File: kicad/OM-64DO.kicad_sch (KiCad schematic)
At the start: 30 parts, among them J101 15EDGVC-3.5-4P, J102 02x03 1.27, J201 15EDGVC-3.5-20P, J301 15EDGVC-3.5-20P, J401 15EDGVC-3.5-20P, J501 15EDGVC-3.5-20P, U101 R-78E3.3-0.5, U102 THVD1450DRBR, U103 STM32G031F8P6

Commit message: feat: add LCSC parts numbers
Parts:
- C101, C102: LCSC# (none) -> C417124; Mouser Part Number 81-GRT31CR61H106KE1L -> (none); Mouser# (none) -> 81-GRT31CR61H106KE1L
- C103, C105, C106: LCSC# (none) -> C161115; Mouser Part Number 81-GCJ188R71H104KA2D -> (none); Mouser# (none) -> 81-GCJ188R71H104KA2D
- C104: LCSC# (none) -> C668370; Mouser Part Number 81-GRT188R61H225KE3D -> (none); Mouser# (none) -> 81-GRT188R61H225KE3D
- D101: LCSC# (none) -> C172881; Mouser Part Number 576-SM712-02HTG -> (none); Mouser# (none) -> 576-SM712-02HTG
- D102: LCSC# (none) -> C364560; Mouser Part Number 859-LTST-C190EKT -> (none); Mouser# (none) -> 859-LTST-C190EKT
- D103: LCSC# (none) -> C6877135; Mouser Part Number 652-CD123D-B140LR -> (none); Mouser# (none) -> 652-CD123D-B140LR
- D104: LCSC# (none) -> C148227; Mouser Part Number 576-SMAJ28A -> (none); Mouser# (none) -> 576-SMAJ28A
- F101: LCSC# (none) -> C151133; Mouser Part Number 576-0466.500NR -> (none); Mouser# (none) -> 576-0466.500NR
- J101: LCSC# (none) -> C22380434
- J201, J301, J401, J501: LCSC# (none) -> C5188336
- R101, R102: LCSC# (none) -> C4297913; Mouser Part Number 667-ERJ-H3EF1002V -> (none); Mouser# (none) -> 667-ERJ-H3EF1002V
- R103: LCSC# (none) -> C491199; Mouser Part Number 667-ERJ-UP3J471V -> (none); Mouser# (none) -> 667-ERJ-UP3J471V
- U101: LCSC# (none) -> C18212316; Mouser Part Number 919-R-78E3.3-0.5 -> (none); Mouser# (none) -> 919-R-78E3.3-0.5
- U102: LCSC# (none) -> C1850226; Mouser Part Number 595-THVD1450DRBR -> (none); Mouser# (none) -> 595-THVD1450DRBR
- U103: LCSC# (none) -> C529334; Mouser Part Number 511-STM32G031F8P6 -> (none); Mouser# (none) -> 511-STM32G031F8P6
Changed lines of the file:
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@@
 			)
 		)
-		(property "Mouser Part Number" "81-GCJ188R71H104KA2D"
+		(property "LCSC#" "C161115"
+			(at 58.42 138.43 90)
+			(effects
+				(font
+					(size 1.27 1.27)
+				)
+				(hide yes)
+			)
+		)
+		(property "Mouser#" "81-GCJ188R71H104KA2D"
 			(at 58.42 138.43 90)
 			(effects
@@
 			)
 		)
-		(property "Mouser Part Number" "81-GCJ188R71H104KA2D"
+		(property "LCSC#" "C161115"
+			(at 186.69 201.93 0)
+			(effects
+				(font
+					(size 1.27 1.27)
+				)
+				(hide yes)
+			)
+		)
+		(property "Mouser#" "81-GCJ188R71H104KA2D"
 			(at 186.69 201.93 0)
 			(effects
@@
 			)
 		)
-		(property "Mouser Part Number" ""
+		(property "LCSC#" ""
 			(at 53.34 87.63 0)
 			(effects
@@
 			)
 		)
-		(property "Mouser Part Number" ""
+		(property "LCSC#" "C5188336"
 			(at 270.51 114.3 0)
 			(effects
@@
 			)
 		)
-		(property "Mouser Part Number" "81-GCJ188R71H104KA2D"
+		(property "LCSC#" "C161115"
+			(at 138.43 115.57 0)
+			(effects
+				(font
+					(size 1.27 1.27)
+				)
+				(hide yes)
+			)
+		)
+		(property "Mouser#" "81-GCJ188R71H104KA2D"
 			(at 138.43 115.57 0)
 			(effects
@@
 			)
 		)
-		(property "Mouser Part Number" "667-ERJ-UP3J471V"
+		(property "Part Number" "ERJ-UP3J471V"
 			(at 166.37 199.39 90)
 			(effects
@@
 			)
 		)
-		(property "Part Number" "ERJ-UP3J471V"
+		(property "LCSC#" "C491199"
+			(at 166.37 199.39 90)
+			(effects
+				(font
+					(size 1.27 1.27)
+				)
+				(hide yes)
+			)
+		)
+		(property "Mouser#" "667-ERJ-UP3J471V"
 			(at 166.37 199.39 90)
 			(effects
@@
 			)
 		)
-		(property "Mouser Part Number" "595-THVD1450DRBR"
+		(property "LCSC#" "C1850226"
+			(at 63.5 154.94 0)
+			(effects
+				(font
+					(size 1.27 1.27)
+				)
+				(hide yes)
+			)
+		)
+		(property "Mouser#" "595-THVD1450DRBR"
 			(at 63.5 154.94 0)
 			(effects
@@
 			)
 		)
-		(property "Mouser Part Number" "81-GRT31CR61H106KE1L"
+		(property "LCSC#" "C417124"
+			(at 129.54 201.93 0)
+			(effects
+				(font
+					(size 1.27 1.27)
+				)
+				(hide yes)
+			)
+		)
+		(property "Mouser#" "81-GRT31CR61H106KE1L"
 			(at 129.54 201.93 0)
 			(effects
@@
 			)
 		)
-		(property "Mouser Part Number" "81-GRT31CR61H106KE1L"
+		(property "LCSC#" "C417124"
+			(at 157.48 201.93 0)
+			(effects
+				(font
+					(size 1.27 1.27)
+				)
+				(hide yes)
+			)
+		)
+		(property "Mouser#" "81-GRT31CR61H106KE1L"
 			(at 157.48 201.93 0)
 			(effects
@@
 			)
 		)
-		(property "Mouser Part Number" ""
+		(property "LCSC#" ""
 			(at 53.34 106.68 0)
 			(effects
@@
 			)
 		)
-		(property "Mouser Part Number" "511-STM32G031F8P6"
+		(property "LCSC#" "C529334"
+			(at 167.64 124.46 0)
+			(effects
+				(font
+					(size 1.27 1.27)
+				)
+				(hide yes)
+			)
+		)
+		(property "Mouser#" "511-STM32G031F8P6"
 			(at 167.64 124.46 0)
 			(effects
@@
 			)
 		)
-		(property "Mouser Part Number" ""
+		(property "LCSC#" ""
 			(at 83.82 201.93 0)
 			(effects
@@
 			)
 		)
-		(property "Mouser Part Number" "576-SM712-02HTG"
+		(property "LCSC#" "C172881"
+			(at 81.28 149.86 90)
+			(effects
+				(font
+					(size 1.27 1.27)
+				)
+				(hide yes)
+			)
+		)
+		(property "Mouser#" "576-SM712-02HTG"
 			(at 81.28 149.86 90)
 			(effects
@@
 			)
 		)
-		(property "Sim.Pin" "1=K 2=A"
+		(property "Part Number" "LTST-C190EKT"
 			(at 166.37 204.47 0)
 			(effects
@@
 			)
 		)
-		(property "Part Number" "LTST-C190EKT"
+		(property "Manufacturer" "LITEON"
 			(at 166.37 204.47 0)
 			(effects
@@
 			)
 		)
-		(property "Mouser Part Number" "859-LTST-C190EKT"
+		(property "LCSC#" "C364560"
 			(at 166.37 204.47 0)
 			(effects
@@
 			)
 		)
-		(property "Manufacturer" "LITEON"
+		(property "Mouser#" "859-LTST-C190EKT"
 			(at 166.37 204.47 0)
 			(effects
@@
 			)
 		)
-		(property "Mouser Part Number" ""
+		(property "LCSC#" ""
 			(at 53.34 113.03 0)
 			(effects
@@
 			)
 		)
-		(property "Mouser Part Number" ""
-			(at 48.26 200.66 0)
+		(property "LCSC#" "C22380434"
+			(at 48.26 200.66 90)
 			(effects
 				(font
@@
 			)
 		)
-		(property "Mouser Part Number" ""
+		(property "LCSC#" ""
 			(at 53.34 93.98 0)
 			(effects
@@
 			)
 		)
-		(property "Mouser Part Number" "576-SMAJ28A"
+		(property "Part Number" "SMAJ28A"
 			(at 121.92 201.93 90)
 			(effects
@@
 			)
 		)
-		(property "Part Number" "SMAJ28A"
+		(property "LCSC#" "C148227"
+			(at 121.92 201.93 90)
+			(effects
+				(font
+					(size 1.27 1.27)
+				)
+				(hide yes)
+			)
+		)
+		(property "Mouser#" "576-SMAJ28A"
 			(at 121.92 201.93 90)
 			(effects
@@
 			)
 		)
-		(property "Mouser Part Number" "919-R-78E3.3-0.5"
+		(property "LCSC#" "C18212316"
+			(at 143.51 198.12 0)
+			(effects
+				(font
+					(size 1.27 1.27)
+				)
+				(hide yes)
+			)
+		)
+		(property "Mouser#" "919-R-78E3.3-0.5"
 			(at 143.51 198.12 0)
 			(effects
@@
 			)
 		)
-		(property "Mouser Part Number" ""
+		(property "LCSC#" "C5188336"
 			(at 270.51 215.9 0)
 			(effects
@@
 			)
 		)
-		(property "Mouser Part Number" "667-ERJ-H3EF1002V"
-			(at 50.8 165.1 0)
+		(property "LCSC#" "C4297913"
+			(at 50.8 165.1 90)
+			(effects
+				(font
+					(size 1.27 1.27)
+				)
+				(hide yes)
+			)
+		)
+		(property "Mouser#" "667-ERJ-H3EF1002V"
+			(at 50.8 165.1 90)
 			(effects
 				(font
@@
 			)
 		)
-		(property "Mouser Part Number" ""
+		(property "LCSC#" ""
 			(at 53.34 100.33 0)
 			(effects
@@
 			)
 		)
-		(property "Mouser Part Number" ""
+		(property "LCSC#" ""
 			(at 53.34 81.28 0)
 			(effects
@@
 			)
 		)
-		(property "Mouser Part Number" ""
+		(property "LCSC#" "C5188336"
 			(at 270.51 165.1 0)
 			(effects
@@
 			)
 		)
-		(property "Mouser Part Number" ""
+		(property "LCSC#" ""
 			(at 53.34 119.38 0)
 			(effects
@@
 			)
 		)
-		(property "Mouser Part Number" "576-0466.500NR"
+		(property "Part Number" "0466.500NR"
 			(at 111.76 198.12 0)
 			(effects
@@
 			)
 		)
-		(property "Part Number" "0466.500NR"
+		(property "LCSC#" "C151133"
+			(at 111.76 198.12 0)
+			(effects
+				(font
+					(size 1.27 1.27)
+				)
+				(hide yes)
+			)
+		)
+		(property "Mouser#" "576-0466.500NR"
 			(at 111.76 198.12 0)
 			(effects
@@
 			)
 		)
-		(property "Mouser Part Number" "652-CD123D-B140LR"
+		(property "Part Number" "CD123D-B140LR"
 			(at 118.11 198.12 0)
 			(effects
@@
 			)
 		)
-		(property "Part Number" "CD123D-B140LR"
+		(property "LCSC#" "C6877135"
+			(at 118.11 198.12 0)
+			(effects
+				(font
+					(size 1.27 1.27)
+				)
+				(hide yes)
+			)
+		)
+		(property "Mouser#" "652-CD123D-B140LR"
 			(at 118.11 198.12 0)
 			(effects
@@
 			)
 		)
-		(property "Mouser Part Number" "667-ERJ-H3EF1002V"
+		(property "LCSC#" "C4297913"
+			(at 223.52 44.45 90)
+			(effects
+				(font
+					(size 1.27 1.27)
+				)
+				(hide yes)
+			)
+		)
+		(property "Mouser#" "667-ERJ-H3EF1002V"
 			(at 223.52 44.45 90)
 			(effects
@@
 			)
 		)
-		(property "Mouser Part Number" ""
+		(property "LCSC#" "C5188336"
 			(at 270.51 63.5 0)
 			(effects
@@
 			)
 		)
-		(property "Mouser Part Number" "81-GRT188R61H225KE3D"
+		(property "LCSC#" "C668370"
+			(at 181.61 201.93 0)
+			(effects
+				(font
+					(size 1.27 1.27)
+				)
+				(hide yes)
+			)
+		)
+		(property "Mouser#" "81-GRT188R61H225KE3D"
 			(at 181.61 201.93 0)
 			(effects

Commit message: feat: reduce board size, update pcb design
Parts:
- U101: symbol Regulator_Switching:R-78E3.3-1.0 -> Converter_DCDC:R-78E3.3-0.5
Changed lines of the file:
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@@
 	(title_block
 		(title "OM-64DO - 64 CHANNEL OUTPUT EXPANSION MODULE (MAIN)")
-		(date "2026-03-09")
+		(date "2026-03-12")
 		(rev "1B")
 		(company "HTTPS://GITHUB.COM/OPENMODBUS/OM-64DO")
@@
 	)
 	(symbol
-		(lib_id "Regulator_Switching:R-78E3.3-1.0")
+		(lib_id "Converter_DCDC:R-78E3.3-0.5")
 		(at 143.51 198.12 0)
 		(unit 1)

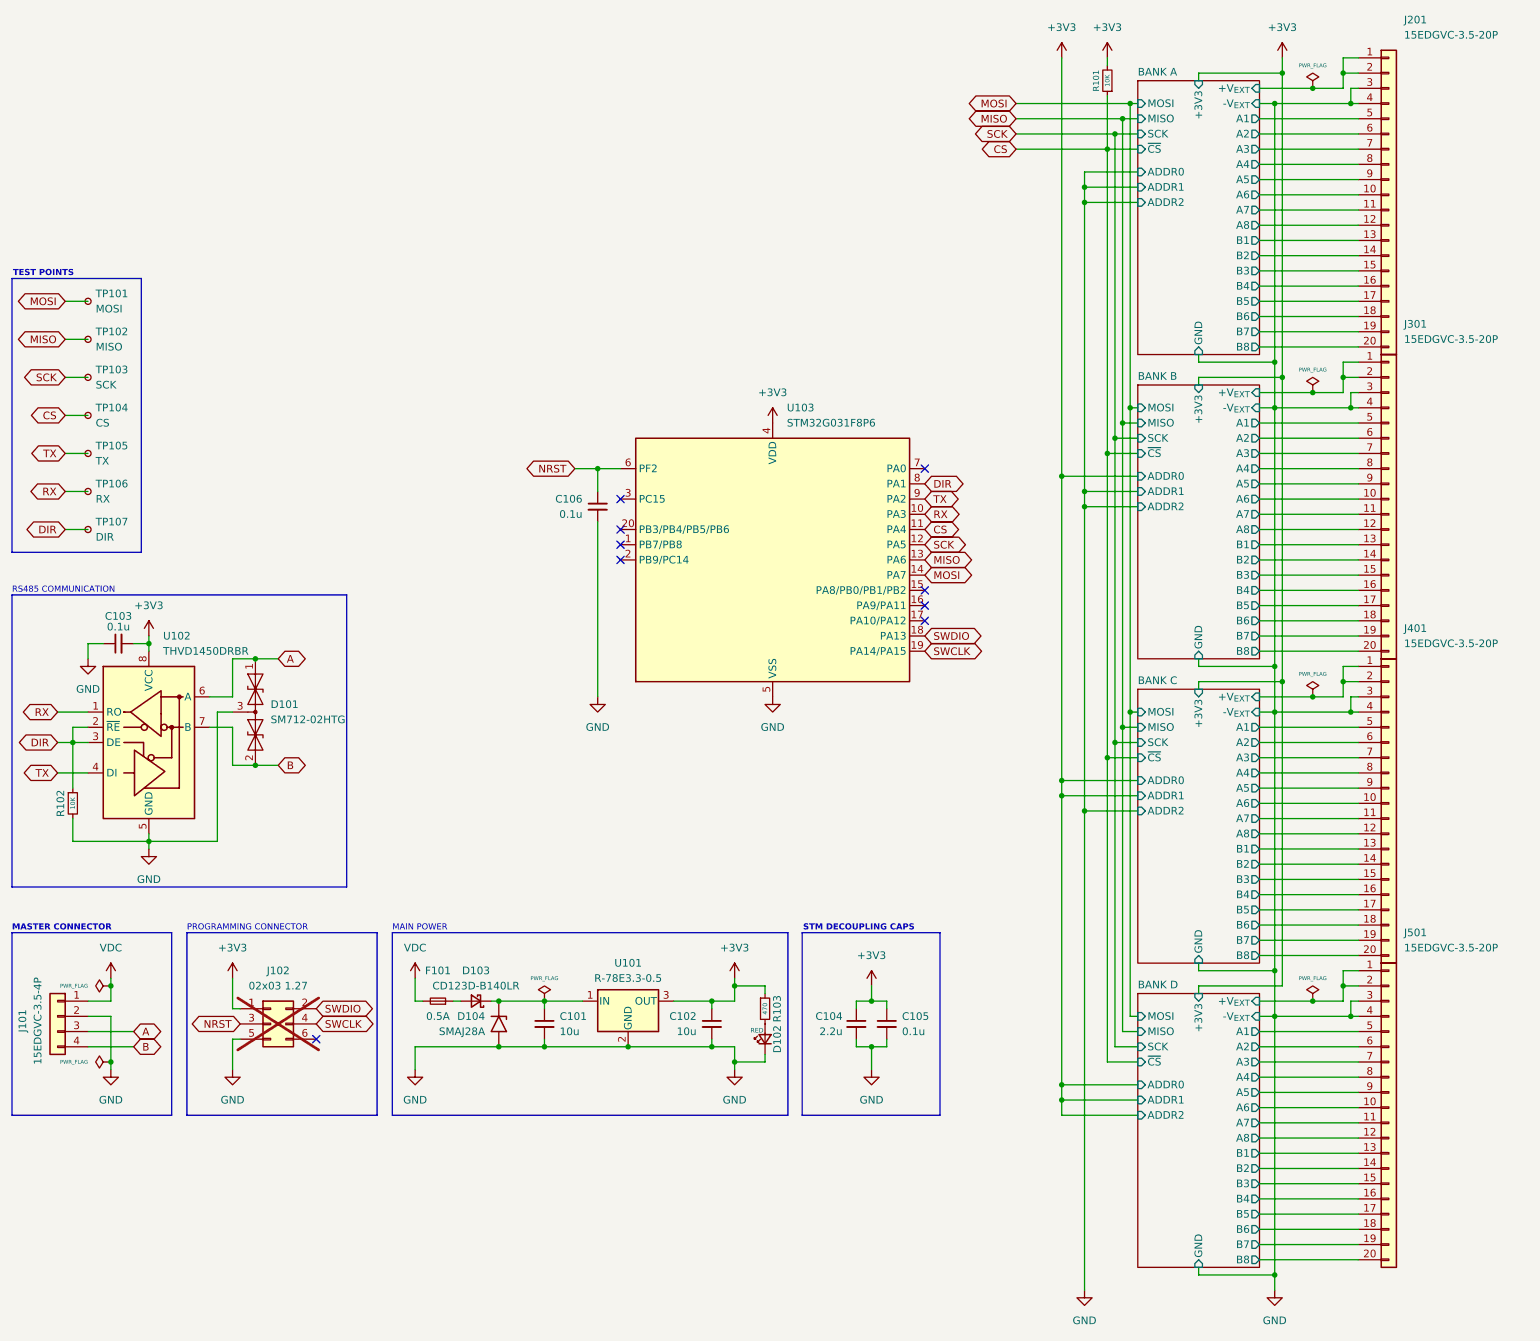
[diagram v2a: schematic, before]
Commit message: feat: add variant with screw connectors
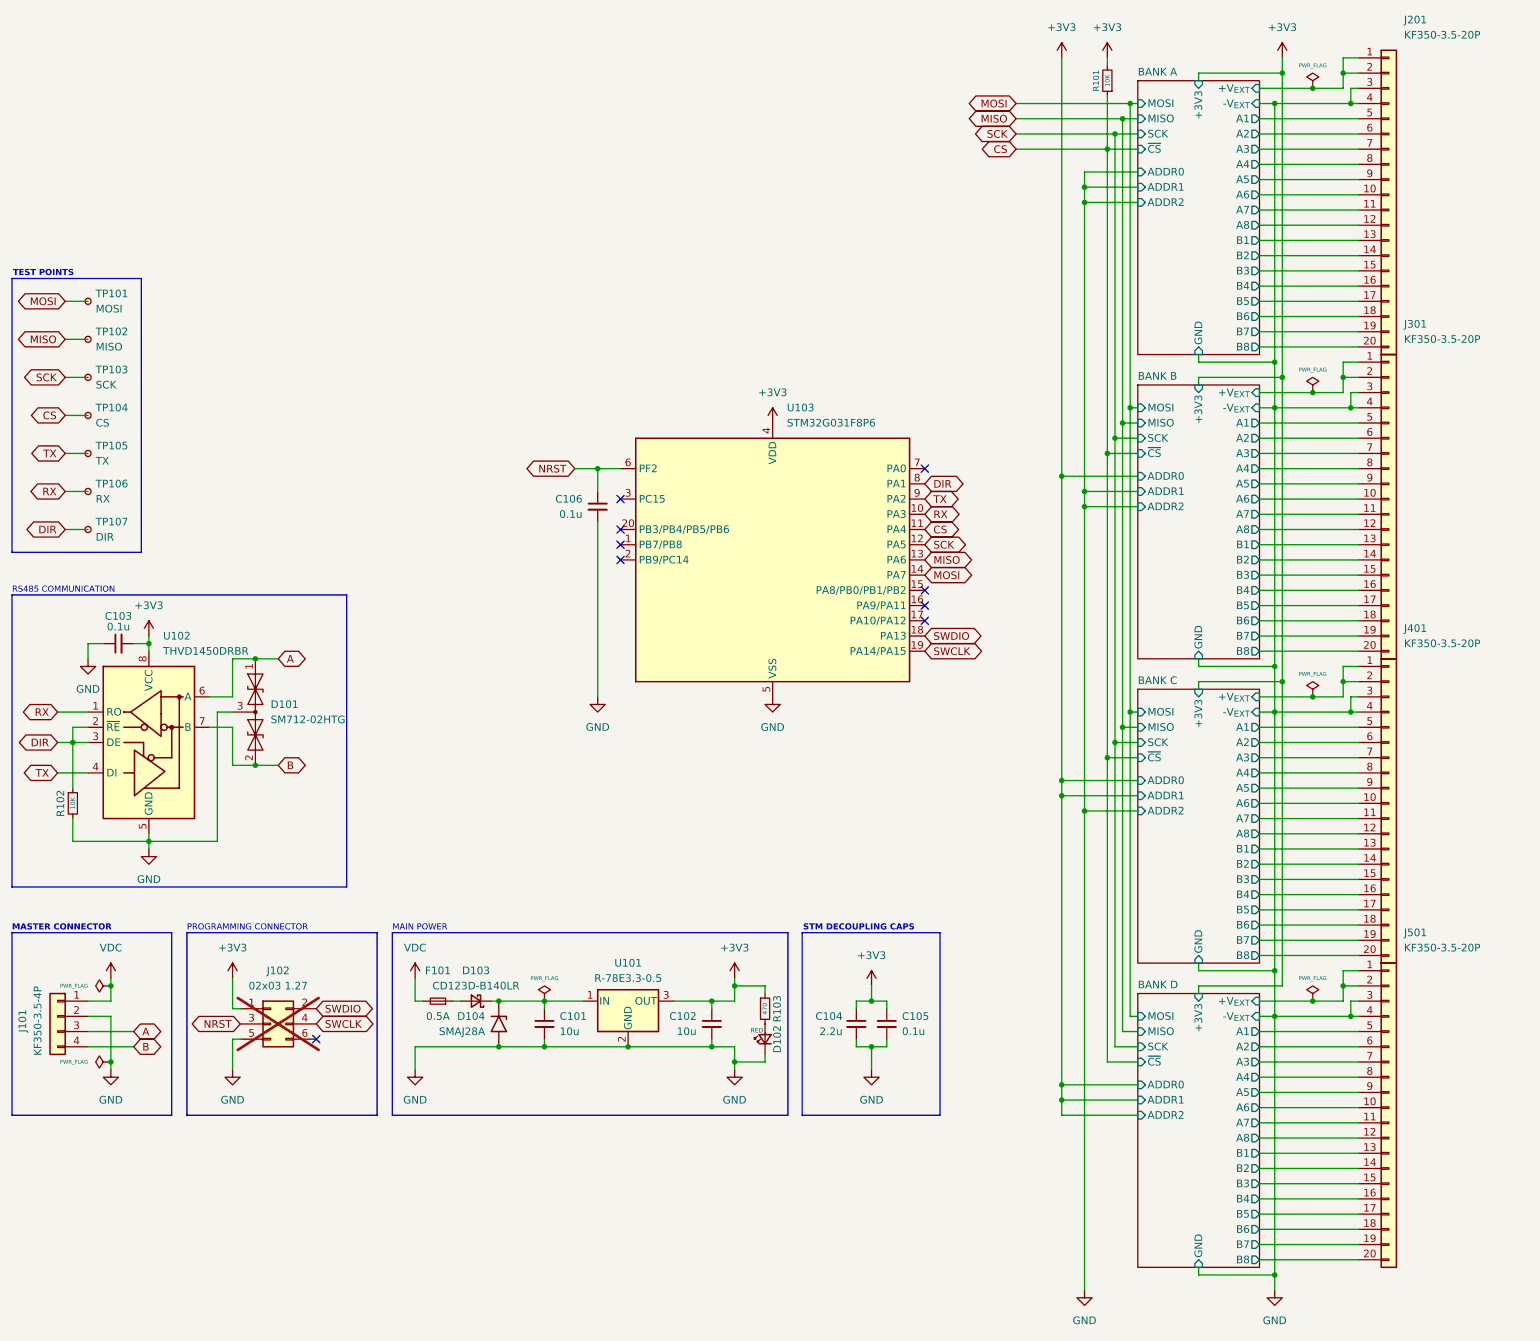
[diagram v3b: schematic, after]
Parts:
- J101: value 15EDGVC-3.5-4P -> KF350-3.5-4P; footprint Project_Library:TerminalBlock_DEGSON_15EDGVC-3.5-4P_No_SilkScreen -> Project_Library:TerminalBlock_KF350-3.5-4P_No_SilkScreen; LCSC# C22380434 -> (none); Manufacturer DEGSON -> KEFA; Part Number 10030000681 -> (none)
- J201, J301, J401, J501: value 15EDGVC-3.5-20P -> KF350-3.5-20P; footprint Project_Library:TerminalBlock_DEGSON_15EDGVC-3.5-20P_No_SilkScreen -> Project_Library:TerminalBlock_KF350-3.5-20P_No_SilkScreen; LCSC# C5188336 -> (none); Manufacturer DEGSON -> KEFA; Part Number 10030000695 -> (none)
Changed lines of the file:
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@@
 			)
 		)
-		(property "Value" "15EDGVC-3.5-20P"
+		(property "Value" "KF350-3.5-20P"
 			(at 273.05 87.63 0)
 			(effects
@@
 			)
 		)
-		(property "Footprint" "Project_Library:TerminalBlock_DEGSON_15EDGVC-3.5-20P_No_SilkScreen"
+		(property "Footprint" "Project_Library:TerminalBlock_KF350-3.5-20P_No_SilkScreen"
 			(at 270.51 114.3 0)
 			(effects
@@
 			)
 		)
-		(property "Description" "Fixed Terminal Blocks"
+		(property "Description" ""
 			(at 270.51 114.3 0)
 			(effects
@@
 			)
 		)
-		(property "Part Number" "10030000695"
+		(property "Part Number" ""
 			(at 270.51 114.3 0)
 			(effects
@@
 			)
 		)
-		(property "Manufacturer" "DEGSON"
+		(property "Manufacturer" "KEFA"
 			(at 270.51 114.3 0)
 			(effects
@@
 			)
 		)
-		(property "LCSC#" "C5188336"
+		(property "LCSC#" ""
 			(at 270.51 114.3 0)
 			(effects
@@
 			)
 		)
-		(property "Value" "15EDGVC-3.5-4P"
+		(property "Value" "KF350-3.5-4P"
 			(at 44.958 201.422 90)
 			(effects
@@
 			)
 		)
-		(property "Footprint" "Project_Library:TerminalBlock_DEGSON_15EDGVC-3.5-4P_No_SilkScreen"
+		(property "Footprint" "Project_Library:TerminalBlock_KF350-3.5-4P_No_SilkScreen"
 			(at 48.26 200.66 0)
 			(effects
@@
 			)
 		)
-		(property "Description" "Generic connector, single row, 01x04, script generated (kicad-library-utils/schlib/autogen/connector/)"
+		(property "Description" ""
 			(at 48.26 200.66 0)
 			(effects
@@
 			)
 		)
-		(property "Part Number" "10030000681"
+		(property "Part Number" ""
 			(at 48.26 200.66 0)
 			(effects
@@
 			)
 		)
-		(property "Manufacturer" "DEGSON"
+		(property "Manufacturer" "KEFA"
 			(at 48.26 200.66 0)
 			(effects
@@
 			)
 		)
-		(property "LCSC#" "C22380434"
+		(property "LCSC#" ""
 			(at 48.26 200.66 90)
 			(effects
@@
 			)
 		)
-		(property "Value" "15EDGVC-3.5-20P"
+		(property "Value" "KF350-3.5-20P"
 			(at 273.05 189.23 0)
 			(effects
@@
 			)
 		)
-		(property "Footprint" "Project_Library:TerminalBlock_DEGSON_15EDGVC-3.5-20P_No_SilkScreen"
+		(property "Footprint" "Project_Library:TerminalBlock_KF350-3.5-20P_No_SilkScreen"
 			(at 270.51 215.9 0)
 			(effects
@@
 			)
 		)
-		(property "Description" "Fixed Terminal Blocks"
+		(property "Description" ""
 			(at 270.51 215.9 0)
 			(effects
@@
 			)
 		)
-		(property "Part Number" "10030000695"
+		(property "Part Number" ""
 			(at 270.51 215.9 0)
 			(effects
@@
 			)
 		)
-		(property "Manufacturer" "DEGSON"
+		(property "Manufacturer" "KEFA"
 			(at 270.51 215.9 0)
 			(effects
@@
 			)
 		)
-		(property "LCSC#" "C5188336"
+		(property "LCSC#" ""
 			(at 270.51 215.9 0)
 			(effects
@@
 			)
 		)
-		(property "Value" "15EDGVC-3.5-20P"
+		(property "Value" "KF350-3.5-20P"
 			(at 273.05 138.43 0)
 			(effects
@@
 			)
 		)
-		(property "Footprint" "Project_Library:TerminalBlock_DEGSON_15EDGVC-3.5-20P_No_SilkScreen"
+		(property "Footprint" "Project_Library:TerminalBlock_KF350-3.5-20P_No_SilkScreen"
 			(at 270.51 165.1 0)
 			(effects
@@
 			)
 		)
-		(property "Description" "Fixed Terminal Blocks"
+		(property "Description" ""
 			(at 270.51 165.1 0)
 			(effects
@@
 			)
 		)
-		(property "Part Number" "10030000695"
+		(property "Part Number" ""
 			(at 270.51 165.1 0)
 			(effects
@@
 			)
 		)
-		(property "Manufacturer" "DEGSON"
+		(property "Manufacturer" "KEFA"
 			(at 270.51 165.1 0)
 			(effects
@@
 			)
 		)
-		(property "LCSC#" "C5188336"
+		(property "LCSC#" ""
 			(at 270.51 165.1 0)
 			(effects
@@
 			)
 		)
-		(property "Value" "15EDGVC-3.5-20P"
+		(property "Value" "KF350-3.5-20P"
 			(at 273.05 36.83 0)
 			(effects
@@
 			)
 		)
-		(property "Footprint" "Project_Library:TerminalBlock_DEGSON_15EDGVC-3.5-20P_No_SilkScreen"
+		(property "Footprint" "Project_Library:TerminalBlock_KF350-3.5-20P_No_SilkScreen"
 			(at 270.51 63.5 0)
 			(effects
@@
 			)
 		)
-		(property "Description" "Fixed Terminal Blocks"
+		(property "Description" ""
 			(at 270.51 63.5 0)
 			(effects
@@
 			)
 		)
-		(property "Part Number" "10030000695"
+		(property "Part Number" ""
 			(at 270.51 63.5 0)
 			(effects
@@
 			)
 		)
-		(property "Manufacturer" "DEGSON"
+		(property "Manufacturer" "KEFA"
 			(at 270.51 63.5 0)
 			(effects
@@
 			)
 		)
-		(property "LCSC#" "C5188336"
+		(property "LCSC#" ""
 			(at 270.51 63.5 0)
 			(effects
